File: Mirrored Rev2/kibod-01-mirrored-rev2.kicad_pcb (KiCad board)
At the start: 2 copper layers, 147.3 x 89 mm, 45 parts, among them J1 02x05, J2 02x05, U1 ProMicro

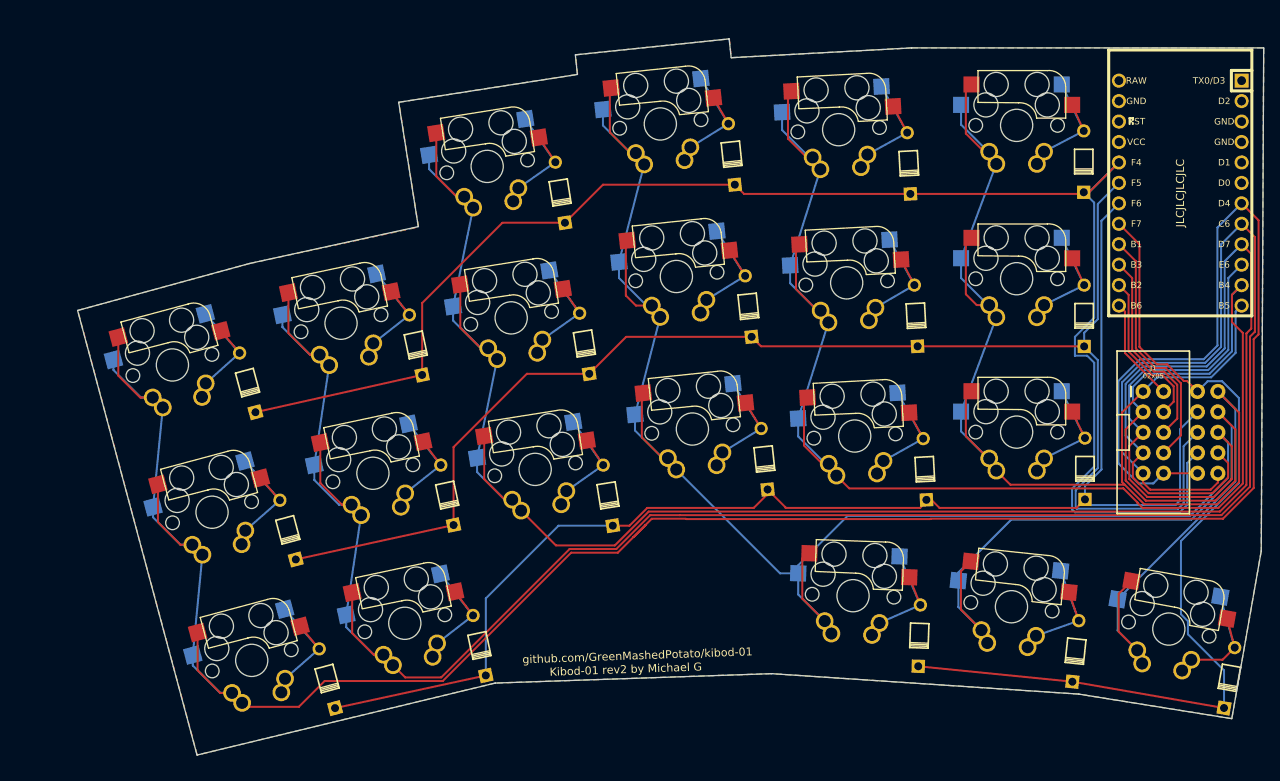
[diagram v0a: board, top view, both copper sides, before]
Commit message: add name and icon, add mounting holes, add trrs support back
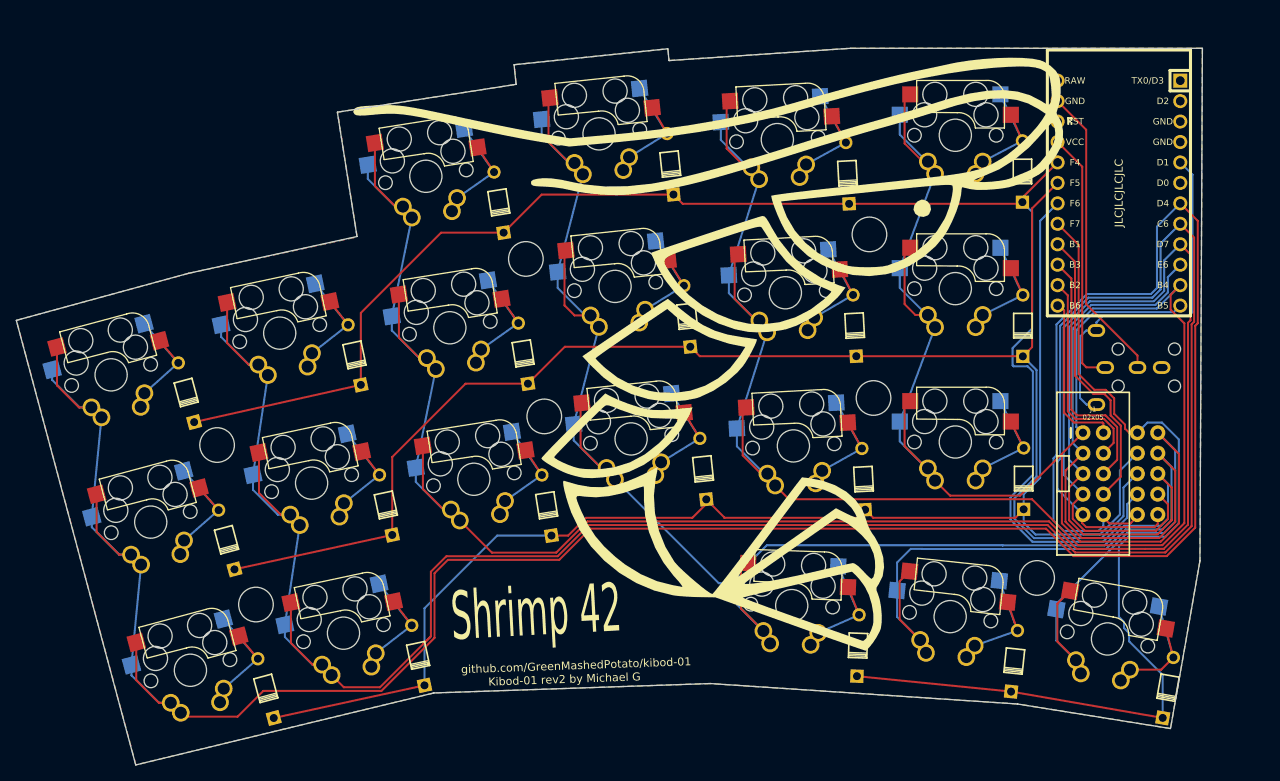
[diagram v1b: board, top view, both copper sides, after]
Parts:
- added G***: LOGO, footprintsGlobal:Shrimp, B.Cu at (105.5, 68.8)
- added Ref**: Val**, footprintsGlobal:hole-m2-pcb, F.Cu at (139.4, 85.8)
- added Ref**: Val**, footprintsGlobal:hole-m2-pcb, F.Cu at (119.1, 63.4)
- added Ref**: Val**, footprintsGlobal:hole-m2-pcb, F.Cu at (118.6, 43.1)
- added Ref**: Val**, footprintsGlobal:hole-m2-pcb, F.Cu at (75.9, 46.2)
- added Ref**: Val**, footprintsGlobal:hole-m2-pcb, F.Cu at (78.2, 65.7)
- added Ref**: Val**, footprintsGlobal:hole-m2-pcb, F.Cu at (37.5, 69.3)
- added Ref**: Val**, footprintsGlobal:hole-m2-pcb, F.Cu at (42.4, 89.1)
- added U2: trrs, footprintsGlobal:trrs, F.Cu at (158.1, 59.7)
- moved J2 9.06 mm to (153.1, 72.8)
- moved J1 9.06 mm to (146.4, 72.8)
- moved D-1-5 7.71 mm to (137.6, 54.5)
- moved D-3-5 7.71 mm to (155.7, 99.4)
- moved K-0-5 7.71 mm to (129.2, 30.8)
- moved K-1-2 7.71 mm to (66.5, 54.7)
- moved D-3-4 7.71 mm to (136.6, 96.1)
- moved K-1-5 7.71 mm to (129.2, 49.9)
- moved K-2-5 7.71 mm to (129.2, 68.9)
- moved K-3-5 7.71 mm to (148.1, 93.4)
- moved D-2-0 7.71 mm to (43.6, 99.5)
- moved K-0-2 7.71 mm to (63.5, 35.9)
- moved D-0-0 7.71 mm to (33.7, 62.8)
- moved D-0-2 7.71 mm to (72.5, 39.2)
- moved D-0-3 7.71 mm to (93.8, 34.4)
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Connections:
- U1 pad 21: unconnected-(U1-Pad21) -> VCC
- U1 pad 23: unconnected-(U1-Pad23) -> GND
- U1 pad 5: unconnected-(U1-Pad5) -> SDA
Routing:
- net SDA: track 0.00 -> 45.1 mm
- net GND: track 0.00 -> 37.2 mm
- net VCC: track 0.00 -> 32.4 mm
- net CL0: track 307.8 -> 326.7 mm
- net CL1: track 283.7 -> 301.3 mm
- net CL4: track 278.9 -> 290.2 mm
- net CL2: track 255.4 -> 266.5 mm
- net CL5: track 201.9 -> 209.2 mm
- net RC3: track 13.0 -> 20.1 mm
- net RC2: track 19.8 -> 26.4 mm
- net RC1: track 25.3 -> 31.8 mm
- net RL0: track 194.9 -> 189.3 mm
- net RC0: track 30.7 -> 36.0 mm
- net RL3: track 114.4 -> 119.0 mm
- net CL3: track 236.4 -> 239.7 mm
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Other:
- outline, holes or cut-outs redrawn
- board text added: "Shrimp 42"

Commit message: cleanup some wiring
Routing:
- net CL0: track 326.7 -> 323.2 mm
- net RL2: track 174.2 -> 175.6 mm
- net CL4: track 290.2 -> 289.0 mm
- net RL0: track 189.3 -> 188.2 mm
- net RL1: track 181.2 -> 180.6 mm

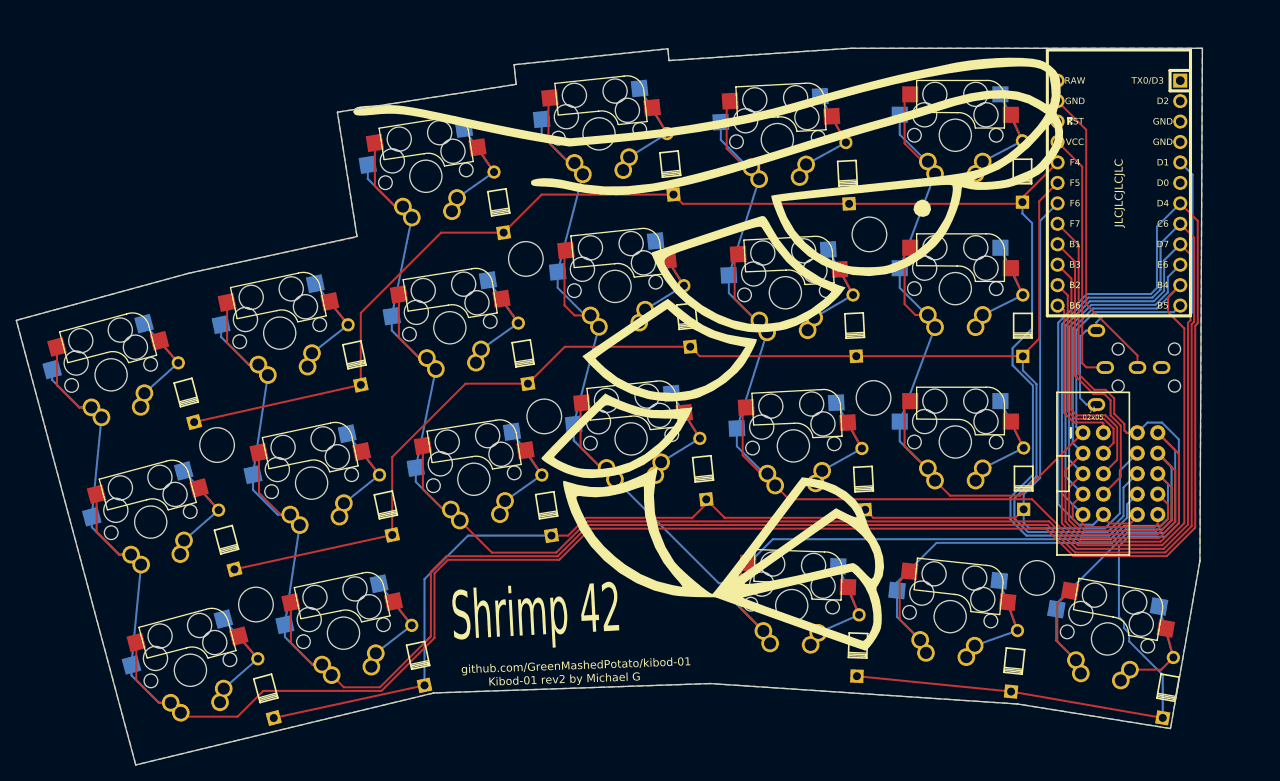
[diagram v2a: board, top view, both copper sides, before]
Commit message: update readme, update wiring
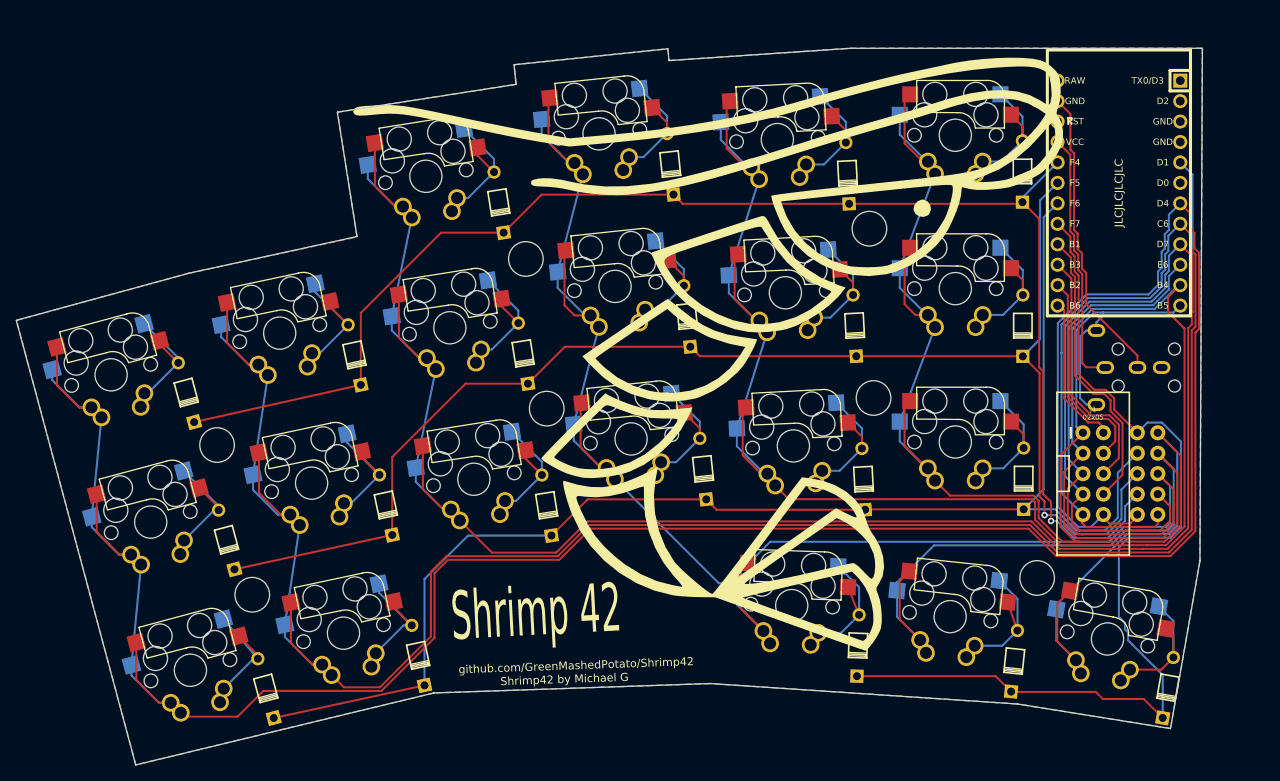
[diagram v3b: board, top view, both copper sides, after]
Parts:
- moved Ref** 1.30 mm to (41.9, 87.9)
- moved Ref** 1.01 mm to (78.5, 64.8)
- moved Ref** 0.71 mm to (118.6, 42.4)
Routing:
- net RL0: track 188.2 -> 181.4 mm, vias 0 -> 1
- net CL5: track 209.2 -> 215.2 mm
- net RL1: track 180.6 -> 176.1 mm, vias 0 -> 1
- net CL4: track 289.0 -> 292.6 mm
- net RC3: track 20.1 -> 18.1 mm
- net RL2: track 175.6 -> 173.6 mm
- net RL3: track 119.2 -> 120.7 mm
- net CL3: track 239.6 -> 241.2 mm
- net Net-(D-1-5-Pad2): track 15.7 -> 17.0 mm
- net Net-(D-2-5-Pad2): track 15.8 -> 17.1 mm
- net CL2: track 266.3 -> 267.6 mm
- net Net-(D-0-5-Pad2): track 15.5 -> 16.7 mm
- net Net-(D-0-4-Pad2): track 15.9 -> 17.1 mm
- net Net-(D-2-4-Pad2): track 15.8 -> 17.0 mm
- net Net-(D-1-4-Pad2): track 15.6 -> 16.8 mm
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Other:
- board text added: "Shrimp42 by Michael G"
- board text added: "github.com/GreenMashedPotato/Shrimp42"
- board text removed: "Kibod-01 rev2 by Michael G"
- board text removed: "github.com/GreenMashedPotato/kibod-01"

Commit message: add support for smd diodes
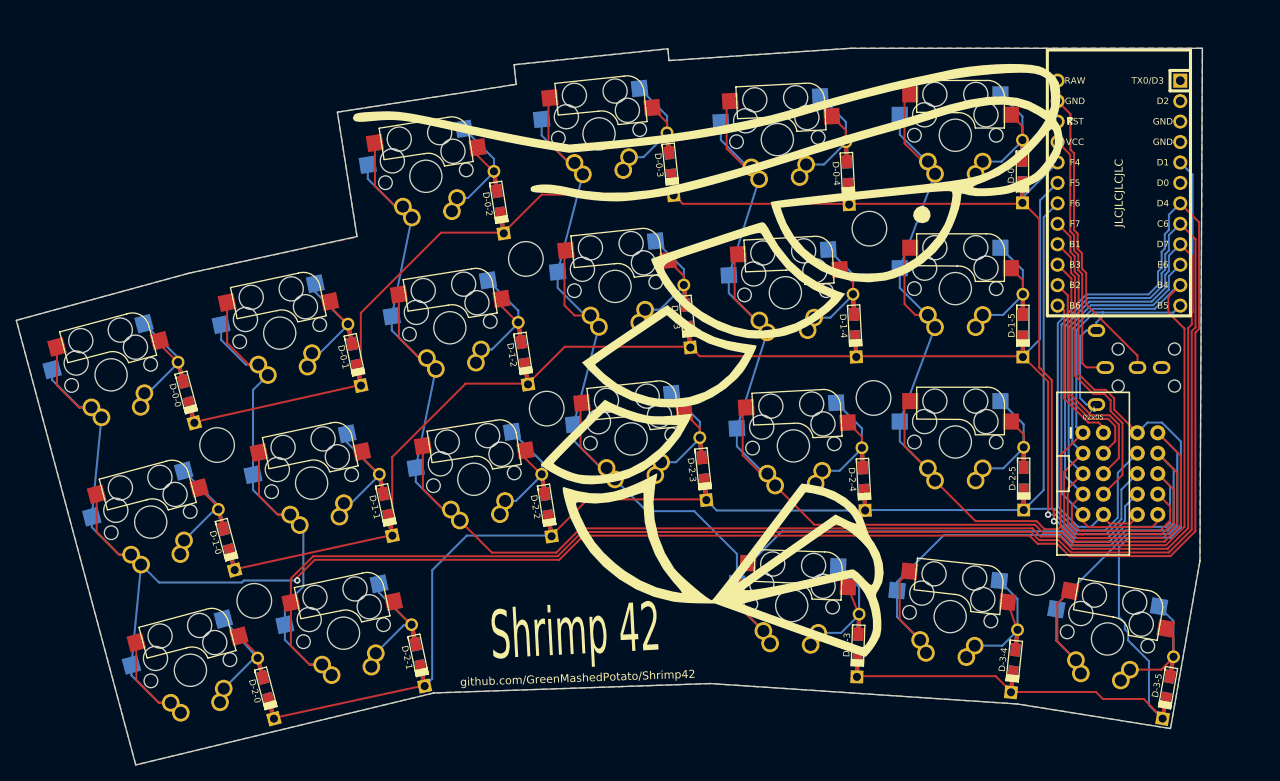
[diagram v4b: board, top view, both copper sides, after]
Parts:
- D-0-0, D-0-1, D-0-2, D-0-3, D-0-4, D-0-5, D-1-0, D-1-1, D-1-2, D-1-3, D-1-4, D-1-5, D-2-0, D-2-1, D-2-2, D-2-3, D-2-4, D-2-5, D-3-3, D-3-4, D-3-5: footprint footprints:diode-vertical -> footprintsGlobal:Diode-dual
- moved Ref** 0.80 mm to (42.2, 88.6)
- moved G*** 0.78 mm to (105.4, 69.6)
- turned D-0-0 to -75 degrees
- turned D-0-1 to -78 degrees
- turned D-0-2 to -81 degrees
- turned D-0-3 to -84 degrees
- turned D-0-4 to -87 degrees
- turned D-0-5 to -90 degrees
- turned D-1-0 to -75 degrees
- turned D-1-1 to -78 degrees
- turned D-1-2 to -81 degrees
- turned D-1-3 to -84 degrees
- turned D-1-4 to -87 degrees
- turned D-1-5 to -90 degrees
- turned D-2-0 to -75 degrees
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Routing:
- net CL0: track 323.3 -> 317.6 mm, vias 0 -> 1
- net CL5: track 215.2 -> 210.4 mm
- net CL3: track 241.2 -> 243.5 mm
- net CL1: track 299.8 -> 297.8 mm
- net Net-(D-1-1-Pad2): track 16.5 -> 14.9 mm
- net Net-(D-0-1-Pad2): track 16.6 -> 15.0 mm
- net Net-(D-0-0-Pad2): track 16.1 -> 14.6 mm
- net Net-(D-1-0-Pad2): track 16.3 -> 14.9 mm
- net Net-(D-2-0-Pad2): track 16.1 -> 15.1 mm
- net RL0: track 181.4 -> 180.6 mm
- net CL4: track 292.6 -> 291.8 mm
- net CL2: track 267.6 -> 266.8 mm
- net Net-(D-2-1-Pad2): track 16.6 -> 15.9 mm
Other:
- board text removed: "Shrimp42 by Michael G"

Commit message: fixed and straightened some wirings
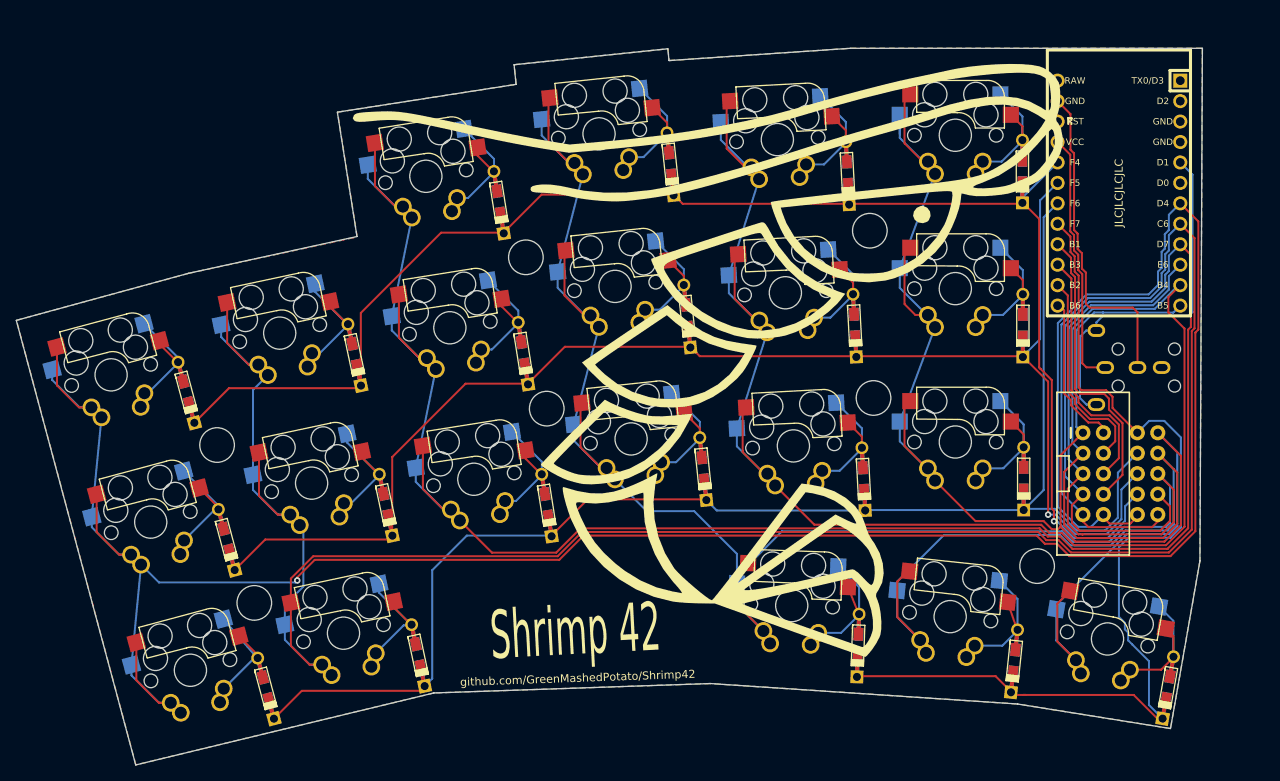
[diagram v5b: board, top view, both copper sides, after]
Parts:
- moved Ref** 1.47 mm to (139.4, 84.3)
- moved Ref** 0.26 mm to (118.6, 42.7)
- moved Ref** 0.25 mm to (42.2, 88.9)
- moved Ref** 0.20 mm to (75.9, 46.0)
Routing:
- net GND: track 37.2 -> 40.4 mm
- net CL5: track 210.4 -> 213.3 mm
- net RL2: track 173.7 -> 175.5 mm
- net RL3: track 120.8 -> 122.5 mm
- net RL0: track 180.6 -> 182.0 mm
- net RL1: track 175.8 -> 177.1 mm
- net RC0: track 36.2 -> 37.1 mm
- net CL4: track 291.8 -> 292.8 mm

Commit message: added case, update readme
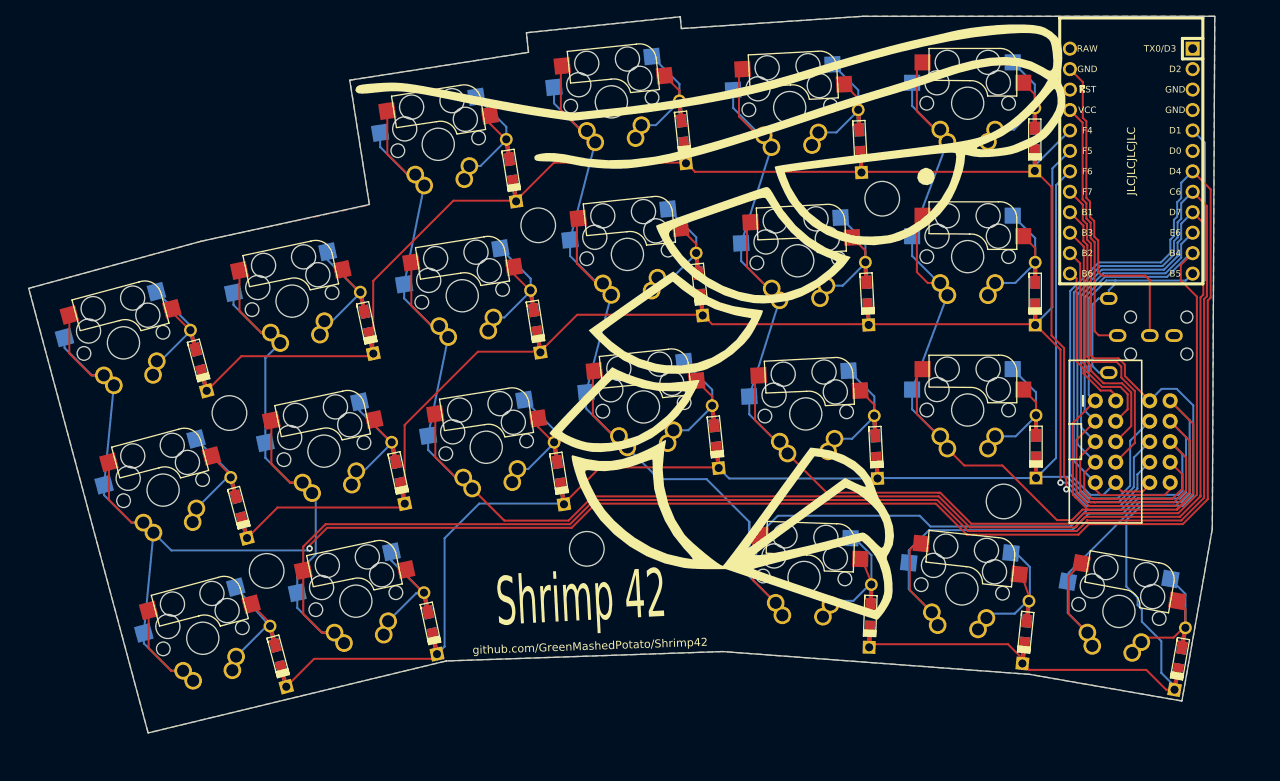
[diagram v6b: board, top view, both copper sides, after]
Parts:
- removed the Ref** at (119.1, 63.4)
- moved Ref** 18.1 mm to (83.5, 82.2)
- moved Ref** 9.04 mm to (135.2, 76.3)
- moved G*** 4.50 mm to (106.4, 65.2), turned to -173 degrees
- moved D-1-5 4.26 mm to (139.2, 50.5)
- moved D-1-0 4.26 mm to (40.2, 77.1)
- moved K-2-0 4.26 mm to (35.8, 93.3)
- moved K-1-0 4.26 mm to (30.8, 74.9)
- moved D-2-3 4.26 mm to (99.4, 68.3)
- moved Ref** 4.26 mm to (43.7, 84.9)
- moved K-1-2 4.26 mm to (68.0, 50.8)
- moved D-0-3 4.26 mm to (95.4, 30.4)
- moved K-0-3 4.26 mm to (86.5, 26.7)
- moved K-0-0 4.26 mm to (25.9, 56.6)
- moved D-0-0 4.26 mm to (35.2, 58.8)
- moved D-0-2 4.26 mm to (74.1, 35.2)
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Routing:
- net CL3: track 243.3 -> 247.7 mm
- net CL5: track 213.3 -> 216.2 mm
- net CL1: track 297.5 -> 298.6 mm
- net CL2: track 266.8 -> 267.9 mm
- net CL0: track 317.5 -> 318.6 mm
- net RL1: track 177.1 -> 176.5 mm
- net RL2: track 175.5 -> 174.9 mm
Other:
- outline, holes or cut-outs redrawn
